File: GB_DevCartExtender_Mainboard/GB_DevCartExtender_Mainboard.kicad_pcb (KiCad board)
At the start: 2 copper layers, 55.5 x 75.3 mm, 3 parts, among them J1 GB_Cart_EdgeConn-1Row-32Pins, J4 Conn_02x16_Odd_Even, J5 Conn_02x16_Odd_Even

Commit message: Modified: PCB routed.
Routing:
- net /AA11: track 0.00 -> 81.7 mm
- net +5V: track 0.00 -> 80.5 mm
- net /AA9: track 0.00 -> 80.4 mm
- net /AA13: track 0.00 -> 80.2 mm
- net /AD7: track 0.00 -> 80.2 mm
- net /AD5: track 0.00 -> 80.0 mm
- net /~AWR: track 0.00 -> 79.8 mm
- net /AD3: track 0.00 -> 79.8 mm
- net /~ASRAM_CS: track 0.00 -> 79.6 mm
- net /AD1: track 0.00 -> 79.6 mm
- net /AAudioIn: track 0.00 -> 79.5 mm
- net /AA1: track 0.00 -> 79.4 mm
- net /AA15: track 0.00 -> 79.4 mm
- net /AA3: track 0.00 -> 79.3 mm
- net /AA5: track 0.00 -> 79.1 mm
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
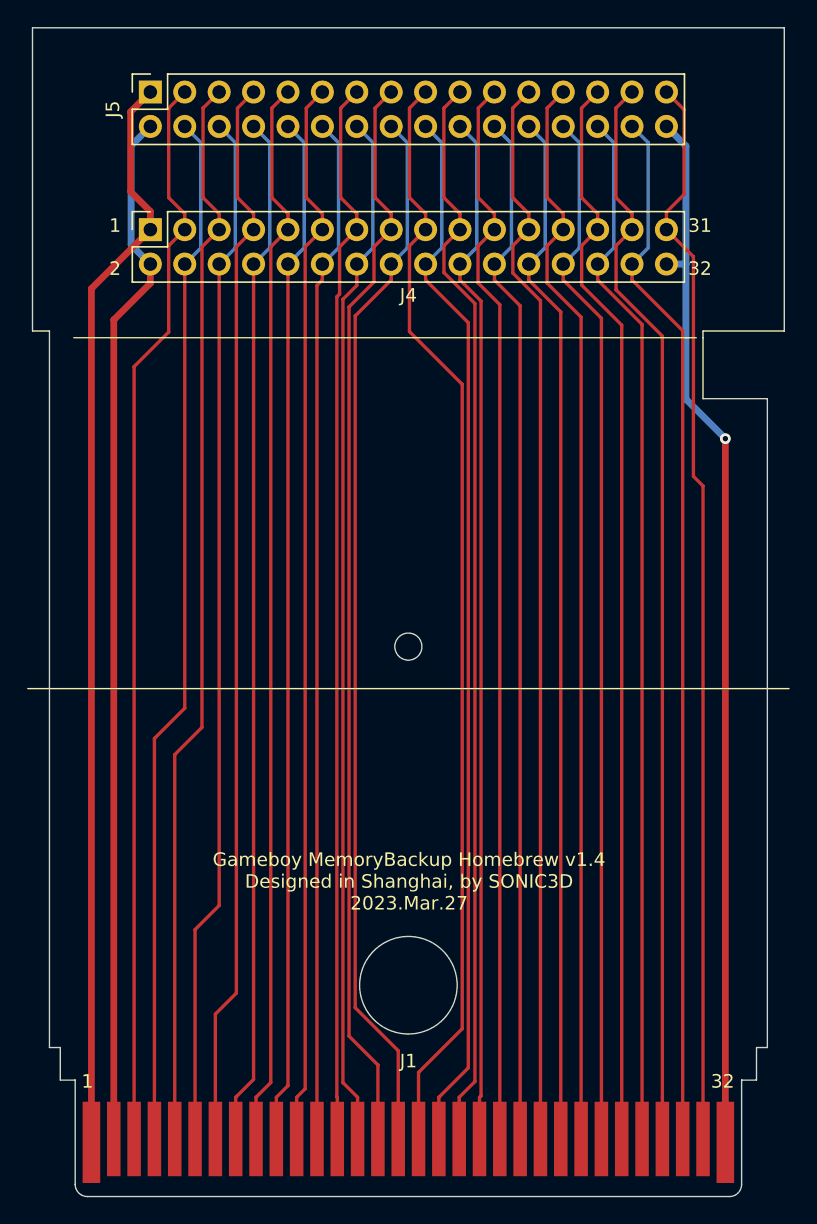
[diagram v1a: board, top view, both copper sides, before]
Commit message: Modified: Filled zone added.
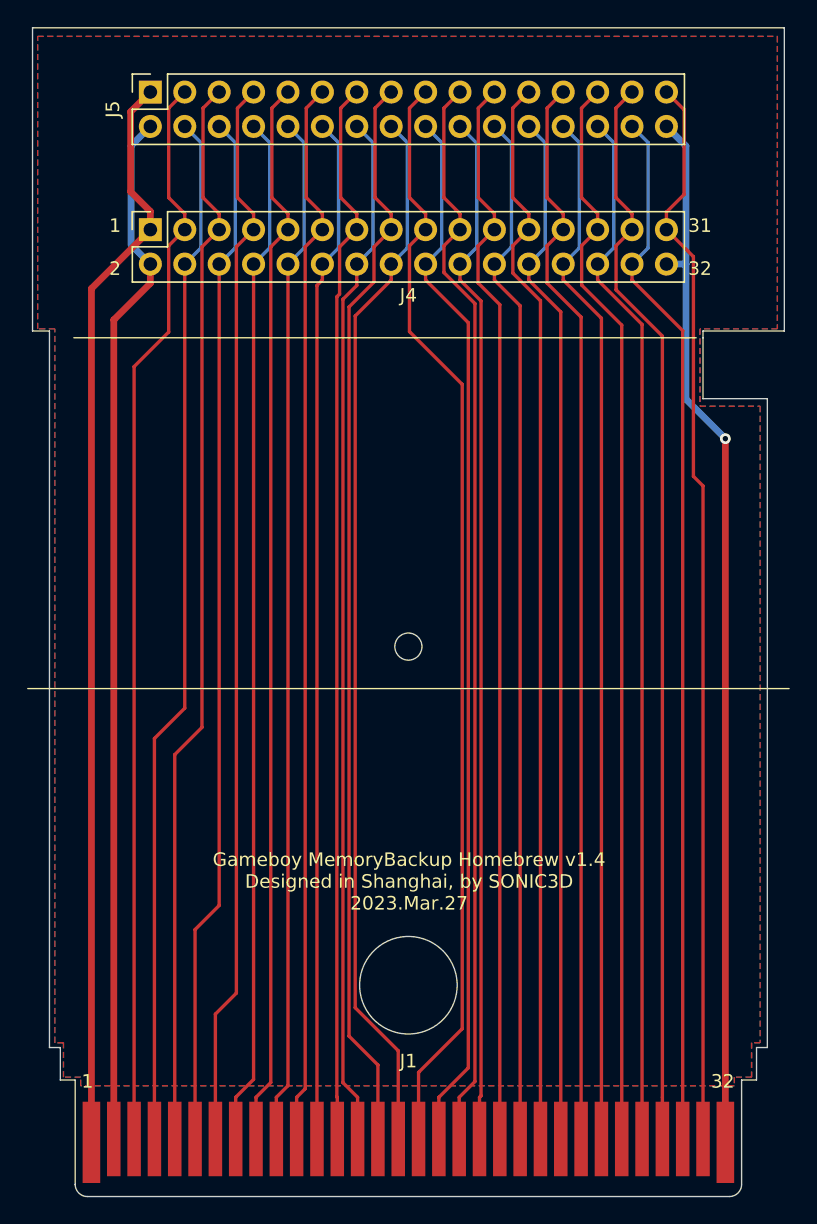
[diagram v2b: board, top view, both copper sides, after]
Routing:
- added copper zone on F.Cu, net +5V
- added copper zone on B.Cu, net GND
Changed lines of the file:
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@@
+    )
+  )
+  (zone (net 1) (net_name +5V) (layer F.Cu) (hatch edge 0.508)
+    (connect_pads (clearance 0.508))
+    (min_thickness 0.254)
+    (fill yes (arc_segments 32) (thermal_gap 0.508) (thermal_bridge_width 0.508))
+    (polygon
+      (pts
+        (xy 116.84 91.44) (xy 111.125 91.44) (xy 111.125 97.155) (xy 115.57 97.155) (xy 115.57 144.145)
+        (xy 114.935 144.145) (xy 114.935 146.685) (xy 113.665 146.685) (xy 113.665 147.32) (xy 65.405 147.32)
+        (xy 65.405 146.685) (xy 64.135 146.685) (xy 64.135 144.145) (xy 63.5 144.145) (xy 63.5 91.44)
+        (xy 62.23 91.44) (xy 62.23 69.85) (xy 116.84 69.85)
+      )
+    )
+  )
+  (zone (net 2) (net_name GND) (layer B.Cu) (hatch edge 0.508)
+    (connect_pads (clearance 0.508))
+    (min_thickness 0.254)
+    (fill yes (arc_segments 32) (thermal_gap 0.508) (thermal_bridge_width 0.508))
+    (polygon
+      (pts
+        (xy 116.84 91.44) (xy 111.125 91.44) (xy 111.125 97.155) (xy 115.57 97.155) (xy 115.57 144.145)
+        (xy 114.935 144.145) (xy 114.935 146.685) (xy 113.665 146.685) (xy 113.665 147.32) (xy 65.405 147.32)
+        (xy 65.405 146.685) (xy 64.135 146.685) (xy 64.135 144.145) (xy 63.5 144.145) (xy 63.5 91.44)
+        (xy 62.23 91.44) (xy 62.23 69.85) (xy 116.84 69.85)
+      )
     )
   )

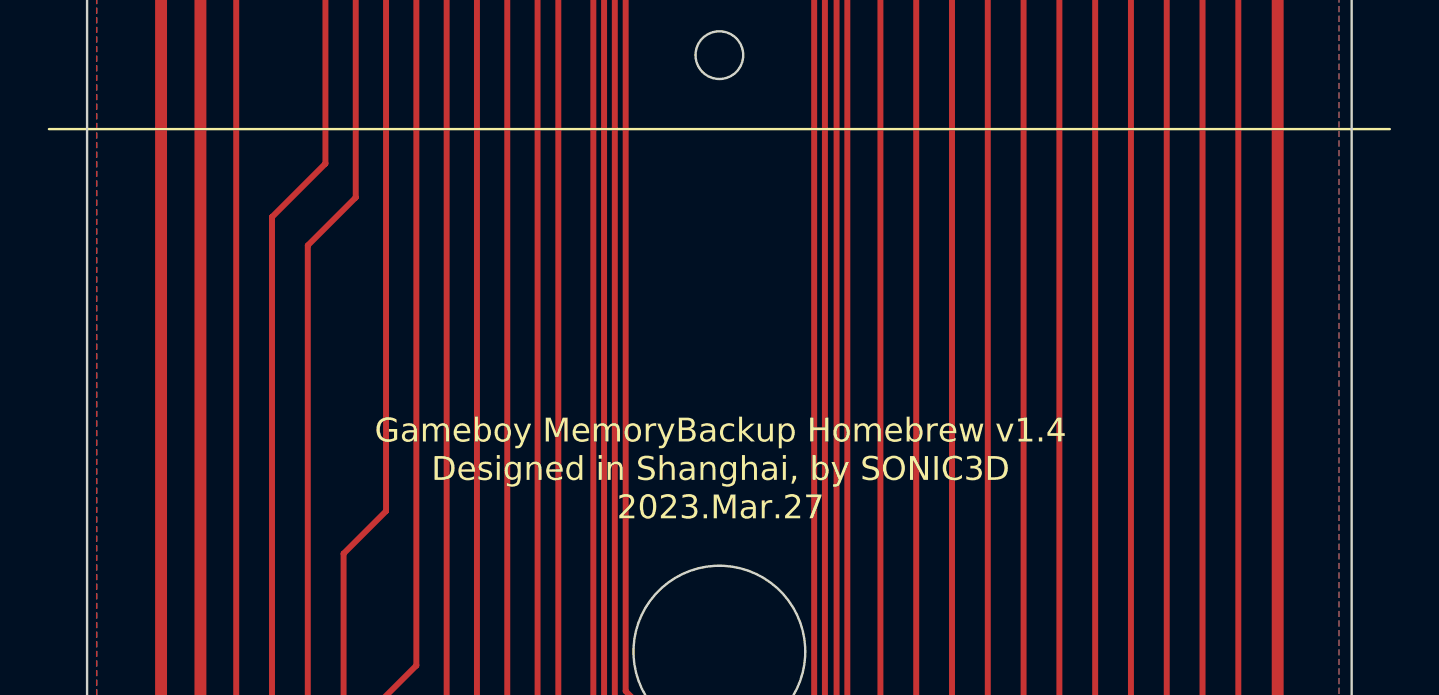
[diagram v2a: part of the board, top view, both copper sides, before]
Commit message: Modified: Logo added.
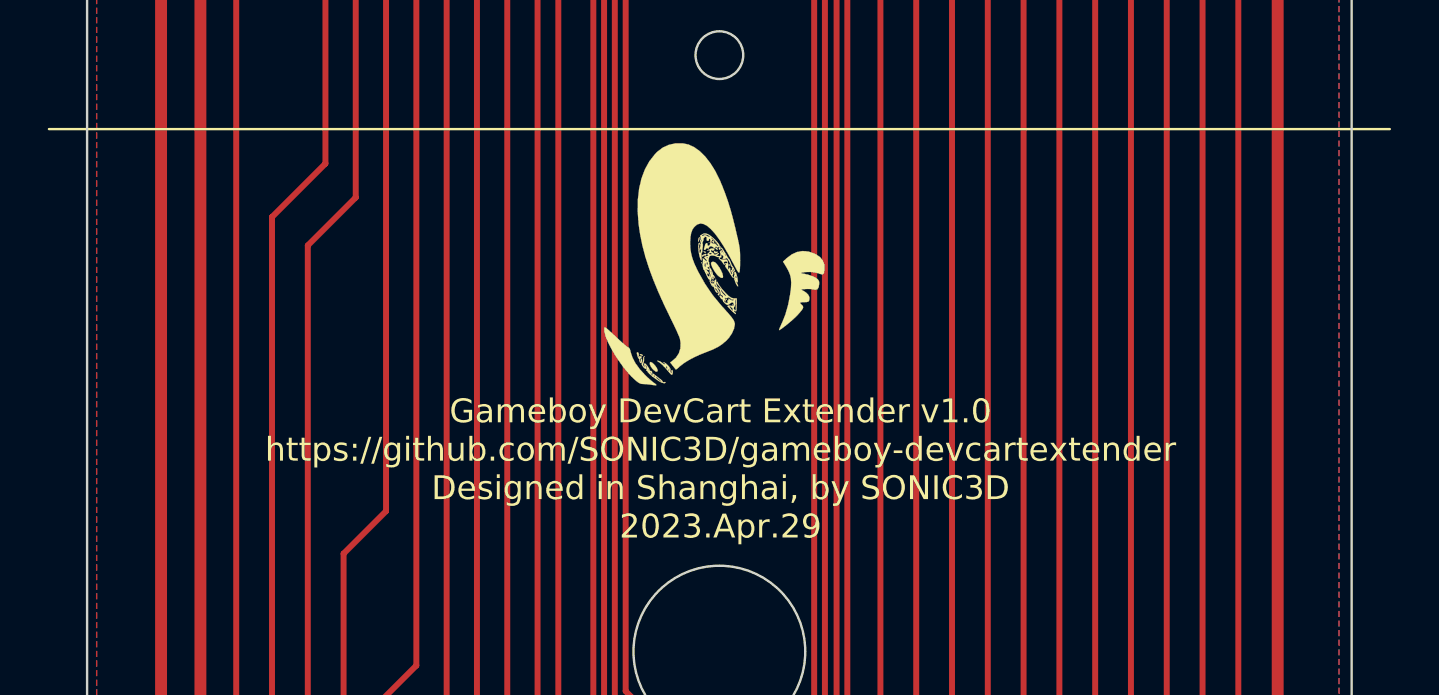
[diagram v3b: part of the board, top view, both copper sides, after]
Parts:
- added G***: LOGO, LogoGraphics:12mm_x_12mm_ShadowSonic, B.Cu at (89.5, 123.8)
- added G***: LOGO, LogoGraphics:12mm_x_12mm_ShadowSonic, F.Cu at (89.5, 123.8)
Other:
- board text added: "Gameboy DevCart Extender v1.0 https://github.com/SONIC3D/gameboy-devcartextender Designed in Shanghai, by SONIC3D 2023.Apr.29"
- board text removed: "Gameboy MemoryBackup Homebrew v1.4 Designed in Shanghai, by SONIC3D 2023.Mar.27"
- board text removed: "Gameboy MemoryBackup Homebrew v1.4 https://github.com/SONIC3D/gameboy-memorybackup Designed in Shanghai, by SONIC3D 2023.Mar.27"
